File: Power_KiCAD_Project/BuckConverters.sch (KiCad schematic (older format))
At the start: 14 parts, among them U4 LM2678SX-5.0/NOPB, U5 LM2678SX-3.3/NOPB

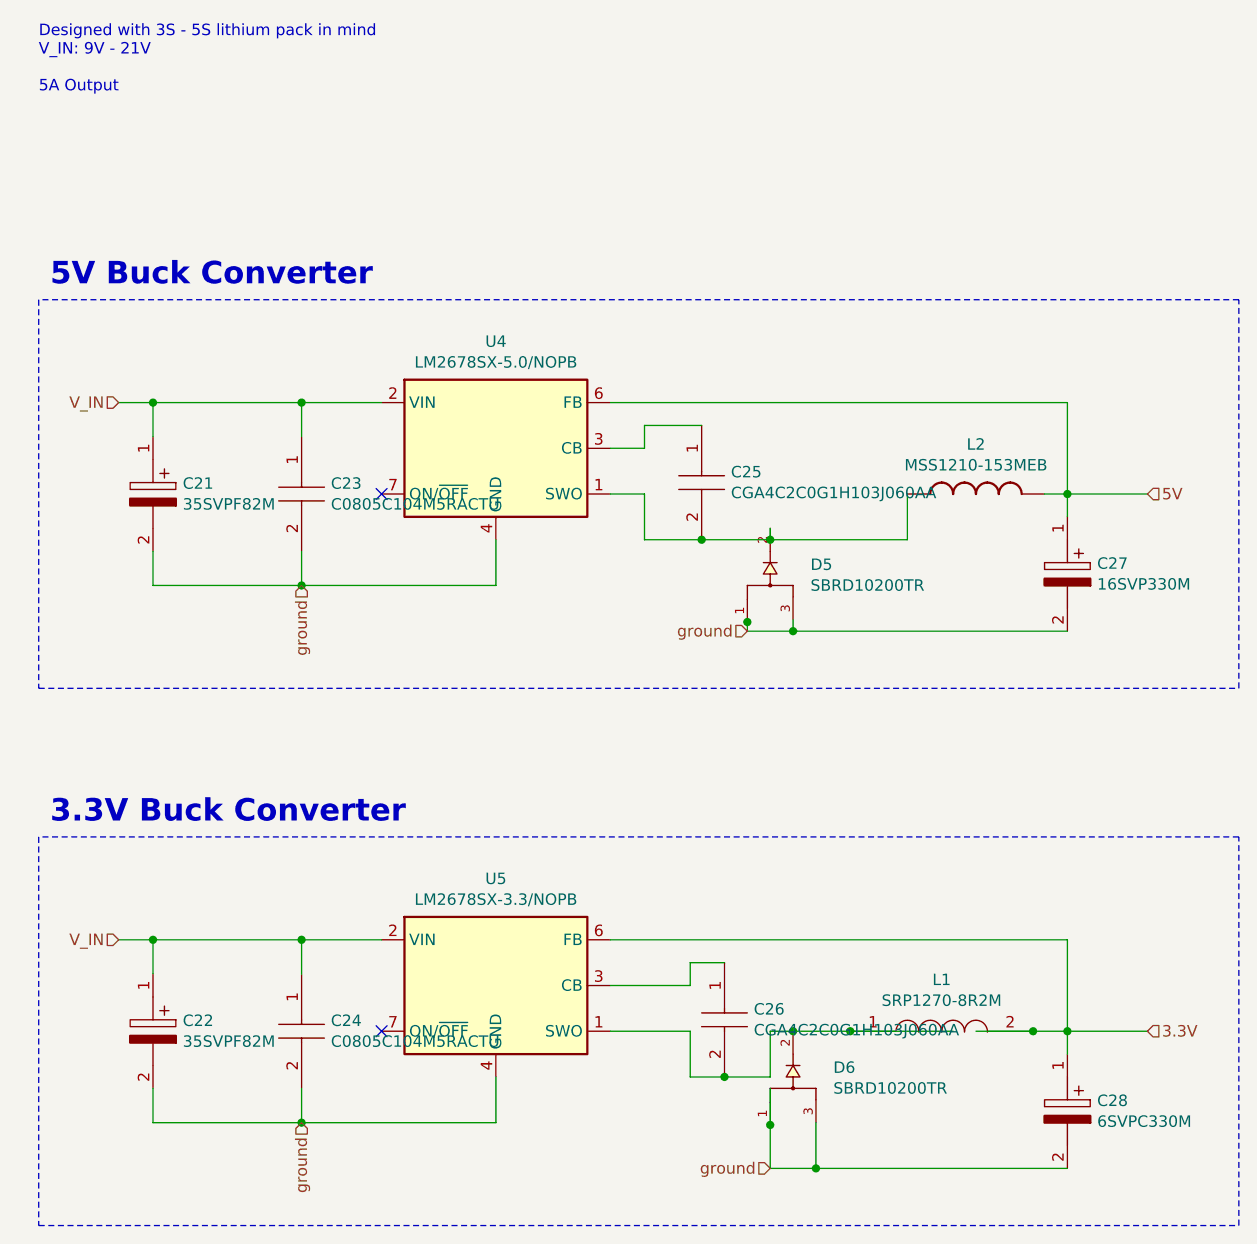
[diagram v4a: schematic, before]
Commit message: Changes to PCB
re did the pcb and added a "switch"
basically its just an xt60 connector in series with the other ones that needs to be shorted for the board to get power
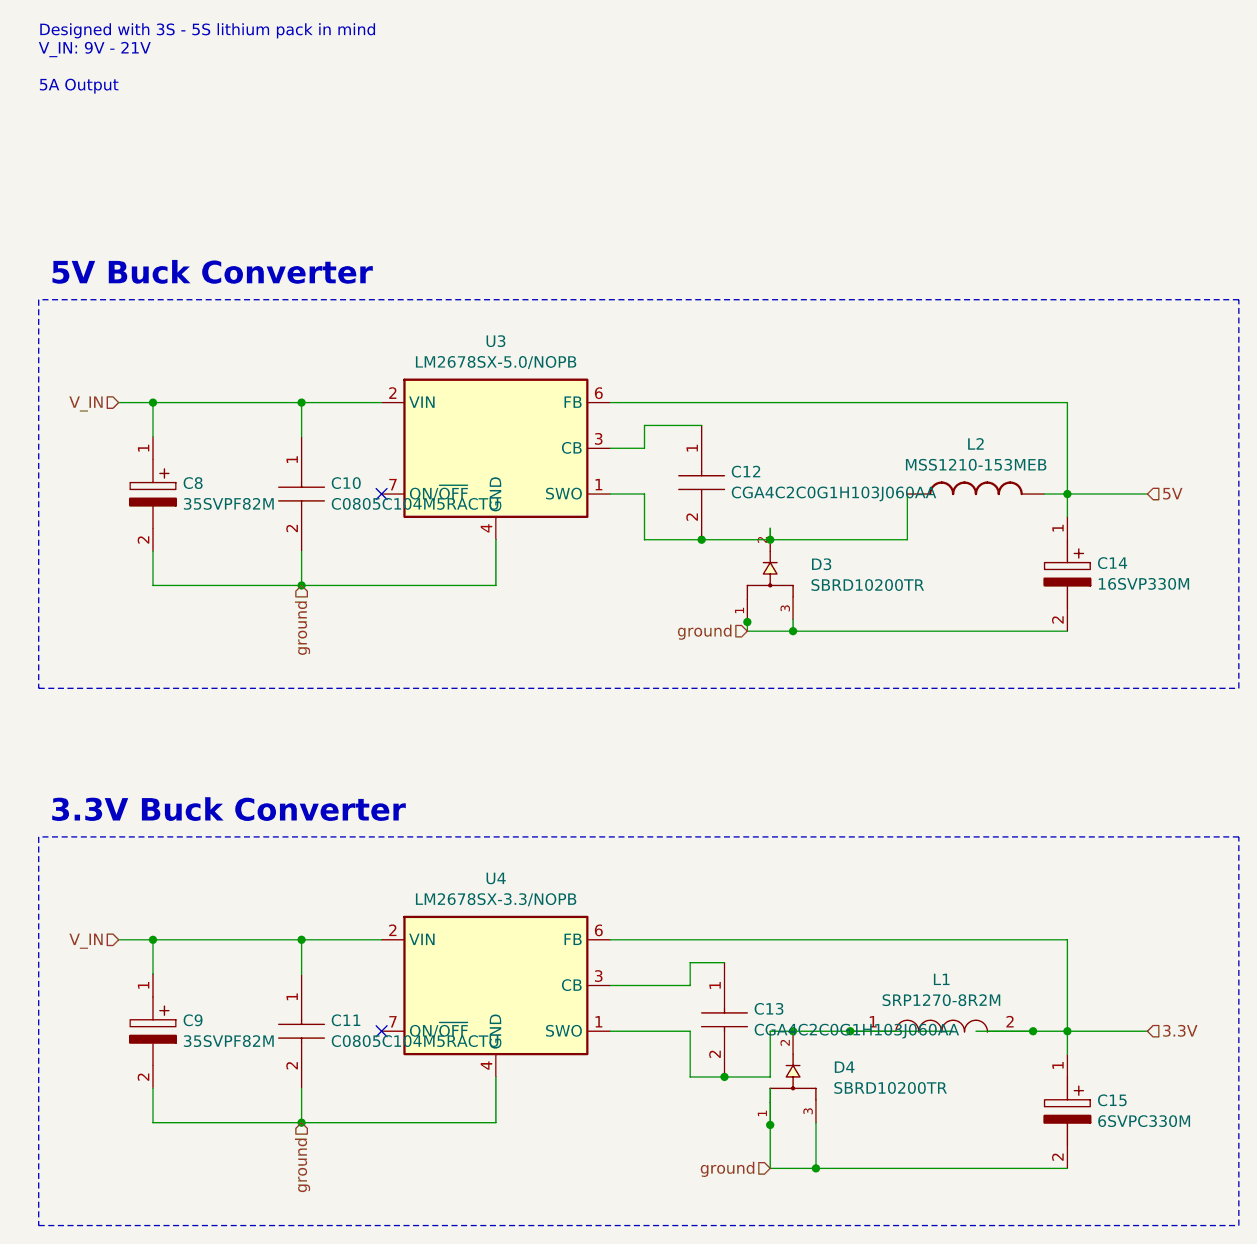
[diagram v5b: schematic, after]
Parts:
- renumbered C23 to C10, C24 to C11, C25 to C12, C26 to C13, C27 to C14, C28 to C15, C21 to C8, C22 to C9, D5 to D3, D6 to D4, U4 to U3, U5 to U4
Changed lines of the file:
@@
 $EndDescr
 $Comp
-L Power_KiCAD_Project-rescue:LM2672M-TO-263-lm2672m-to-263 U5
+L Power_KiCAD_Project-rescue:LM2672M-TO-263-lm2672m-to-263 U4
 U 1 1 61A319C7
 P 4900 5200
-F 0 "U5" H 4900 5667 50  0000 C CNN
+F 0 "U4" H 4900 5667 50  0000 C CNN
 F 1 "LM2678SX-3.3/NOPB" H 4900 5576 50  0000 C CNN
 F 2 "Package_TO_SOT_SMD:TO-263-7_TabPin8" H 4950 4850 50  0001 L CIN
@@
 ground
 $Comp
-L SBRD10200TR:SBRD10200TR D5
+L SBRD10200TR:SBRD10200TR D3
 U 1 1 61A8FF3C
 P 6100 3400
-F 0 "D5" H 6276 3441 50  0000 L CNN
+F 0 "D3" H 6276 3441 50  0000 L CNN
 F 1 "SBRD10200TR" H 6276 3350 50  0000 L CNN
 F 2 "SBRD10200TR:DPAK228P1005X240-4N" H 6100 3400 50  0001 L BNN
@@
 $EndComp
 $Comp
-L SBRD10200TR:SBRD10200TR D6
+L SBRD10200TR:SBRD10200TR D4
 U 1 1 61A94D59
 P 6200 5600
-F 0 "D6" H 6376 5641 50  0000 L CNN
+F 0 "D4" H 6376 5641 50  0000 L CNN
 F 1 "SBRD10200TR" H 6376 5550 50  0000 L CNN
 F 2 "SBRD10200TR:DPAK228P1005X240-4N" H 6200 5600 50  0001 L BNN
@@
 	6200 3650 7400 3650
 $Comp
-L SamacSys_Parts:CGA4C2C0G1H103J060AA C26
+L SamacSys_Parts:CGA4C2C0G1H103J060AA C13
 U 1 1 61BC76DD
 P 5900 5100
-F 0 "C26" V 6104 5228 50  0000 L CNN
+F 0 "C13" V 6104 5228 50  0000 L CNN
 F 1 "CGA4C2C0G1H103J060AA" V 6195 5228 50  0000 L CNN
 F 2 "SamacSys_Parts:CAPC2012X75N" H 6250 5150 50  0001 L CNN
@@
 $EndComp
 $Comp
-L SamacSys_Parts:C0805C104M5RACTU C24
+L SamacSys_Parts:C0805C104M5RACTU C11
 U 1 1 61BC89F9
 P 4050 5150
-F 0 "C24" V 4254 5278 50  0000 L CNN
+F 0 "C11" V 4254 5278 50  0000 L CNN
 F 1 "C0805C104M5RACTU" V 4345 5278 50  0000 L CNN
 F 2 "SamacSys_Parts:CAPC2012X88N" H 4400 5200 50  0001 L CNN
@@
 $EndComp
 $Comp
-L SamacSys_Parts:35SVPF82M C22
+L SamacSys_Parts:35SVPF82M C9
 U 1 1 61BCB4E6
 P 3400 5150
-F 0 "C22" V 3604 5280 50  0000 L CNN
+F 0 "C9" V 3604 5280 50  0000 L CNN
 F 1 "35SVPF82M" V 3695 5280 50  0000 L CNN
 F 2 "SamacSys_Parts:16SVPT560M" H 3750 5200 50  0001 L CNN
@@
 $EndComp
 $Comp
-L SamacSys_Parts:6SVPC330M C28
+L SamacSys_Parts:6SVPC330M C15
 U 1 1 61BCD9CD
 P 7400 5500
-F 0 "C28" V 7604 5630 50  0000 L CNN
+F 0 "C15" V 7604 5630 50  0000 L CNN
 F 1 "6SVPC330M" V 7695 5630 50  0000 L CNN
 F 2 "SamacSys_Parts:16SVF180M" H 7750 5550 50  0001 L CNN
@@
 $EndComp
 $Comp
-L SamacSys_Parts:35SVPF82M C21
+L SamacSys_Parts:35SVPF82M C8
 U 1 1 61BCF050
 P 3400 2800
-F 0 "C21" V 3604 2930 50  0000 L CNN
+F 0 "C8" V 3604 2930 50  0000 L CNN
 F 1 "35SVPF82M" V 3695 2930 50  0000 L CNN
 F 2 "SamacSys_Parts:16SVPT560M" H 3750 2850 50  0001 L CNN
@@
 $EndComp
 $Comp
-L SamacSys_Parts:C0805C104M5RACTU C23
+L SamacSys_Parts:C0805C104M5RACTU C10
 U 1 1 61BD084E
 P 4050 2800
-F 0 "C23" V 4254 2928 50  0000 L CNN
+F 0 "C10" V 4254 2928 50  0000 L CNN
 F 1 "C0805C104M5RACTU" V 4345 2928 50  0000 L CNN
 F 2 "SamacSys_Parts:CAPC2012X88N" H 4400 2850 50  0001 L CNN
@@
 $EndComp
 $Comp
-L SamacSys_Parts:CGA4C2C0G1H103J060AA C25
+L SamacSys_Parts:CGA4C2C0G1H103J060AA C12
 U 1 1 61BD1A0A
 P 5800 2750
-F 0 "C25" V 6004 2878 50  0000 L CNN
+F 0 "C12" V 6004 2878 50  0000 L CNN
 F 1 "CGA4C2C0G1H103J060AA" V 6095 2878 50  0000 L CNN
 F 2 "SamacSys_Parts:CAPC2012X75N" H 6150 2800 50  0001 L CNN
@@
 	7000 5400 7250 5400
 $Comp
-L Power_KiCAD_Project-rescue:LM2672M-TO-263-lm2672m-to-263 U4
+L Power_KiCAD_Project-rescue:LM2672M-TO-263-lm2672m-to-263 U3
 U 1 1 61A7F0DE
 P 4900 2850
-F 0 "U4" H 4900 3317 50  0000 C CNN
+F 0 "U3" H 4900 3317 50  0000 C CNN
 F 1 "LM2678SX-5.0/NOPB" H 4900 3226 50  0000 C CNN
 F 2 "Package_TO_SOT_SMD:TO-263-7_TabPin8" H 4950 2500 50  0001 L CIN
@@
 $EndComp
 $Comp
-L SamacSys_Parts:16SVP330M C27
+L SamacSys_Parts:16SVP330M C14
 U 1 1 61BD32A5
 P 7400 3150
-F 0 "C27" V 7604 3280 50  0000 L CNN
+F 0 "C14" V 7604 3280 50  0000 L CNN
 F 1 "16SVP330M" V 7695 3280 50  0000 L CNN
 F 2 "SamacSys_Parts:16SVF1000M" H 7750 3200 50  0001 L CNN
